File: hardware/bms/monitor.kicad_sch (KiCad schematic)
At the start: 116 parts, among them Q2 Q_PMOS_GDS, Q3 Q_PMOS_GDS, U1 BQ76952

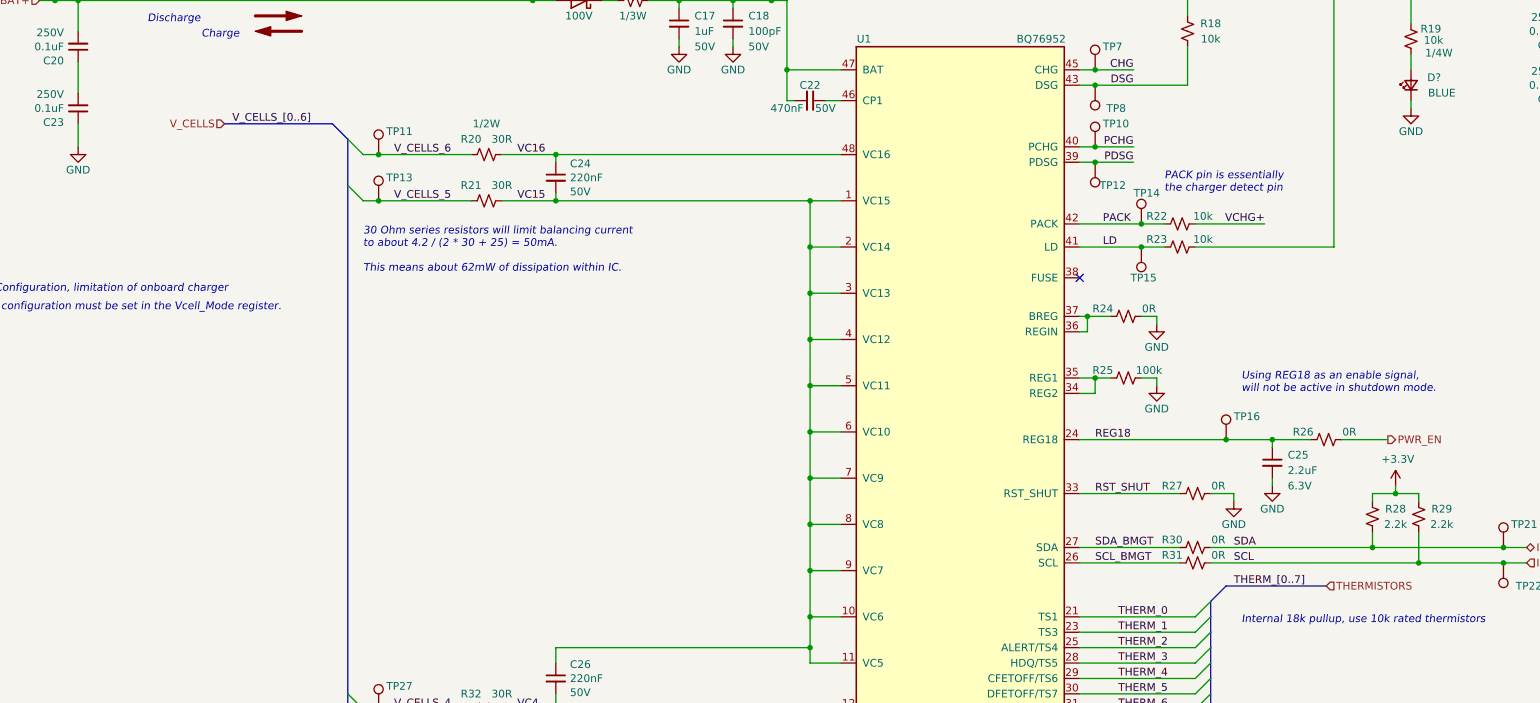
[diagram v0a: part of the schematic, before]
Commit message: Updated USB C connector, fixed all sch ERC errors, imported footprints into pcb file, fixed any pcb import errors.
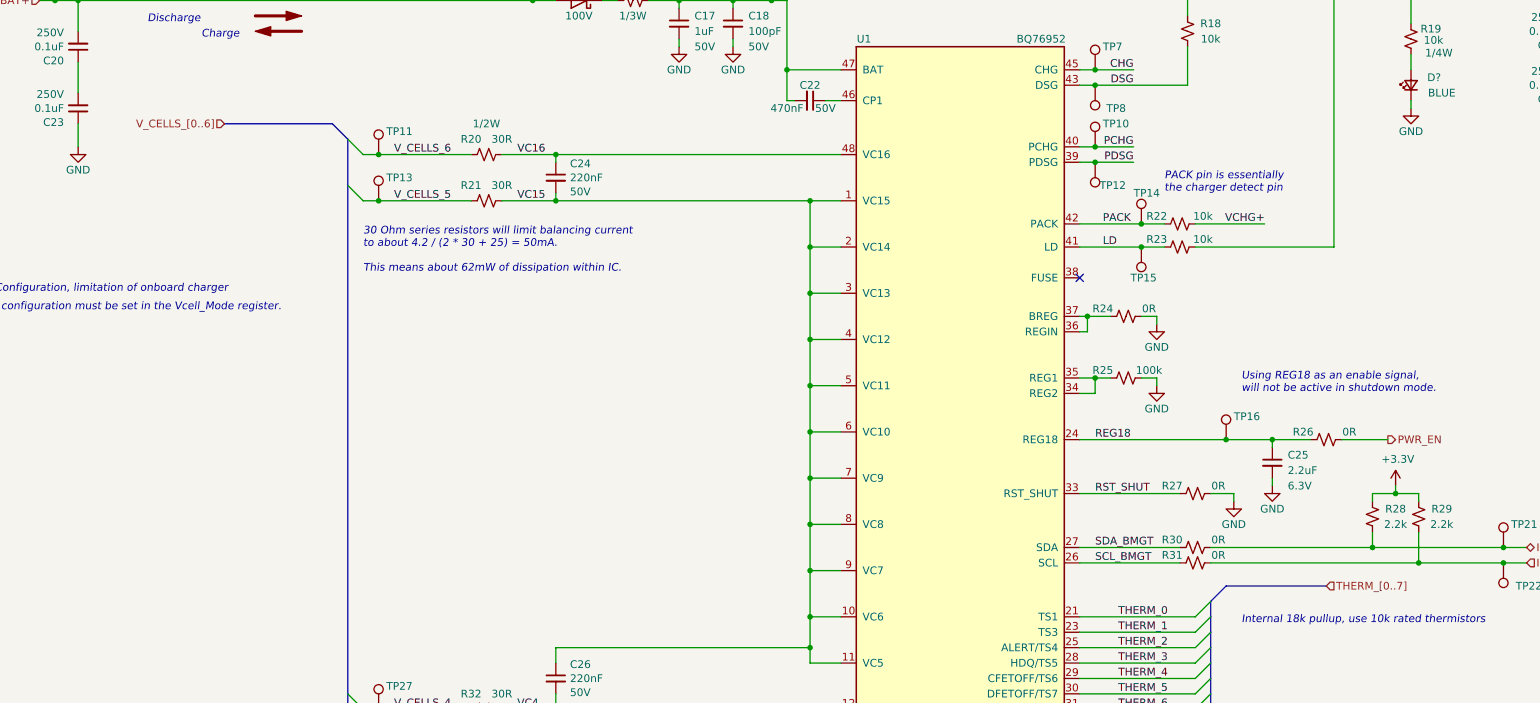
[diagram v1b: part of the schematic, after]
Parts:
- C24, C26, C31, C32, C38, C39, C40: footprint (none) -> Capacitor_SMD:C_0603_1608Metric

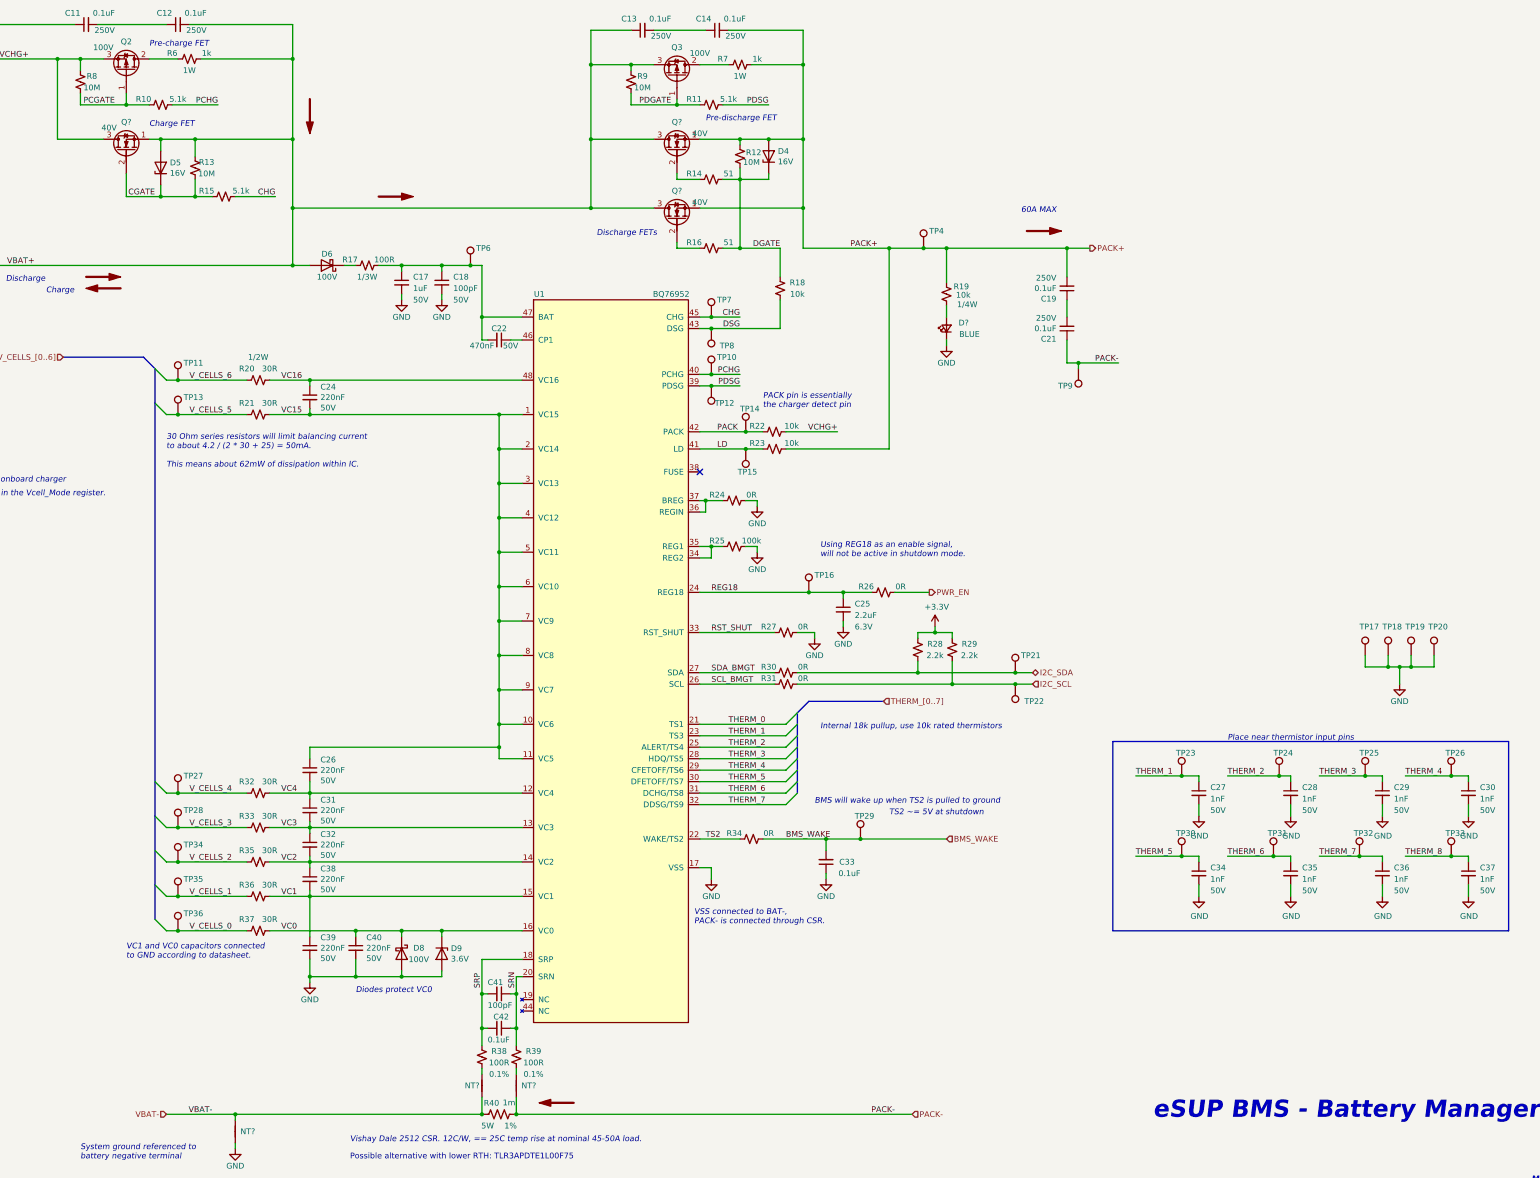
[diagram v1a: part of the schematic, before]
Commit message: Sch cleanup, added extra netties
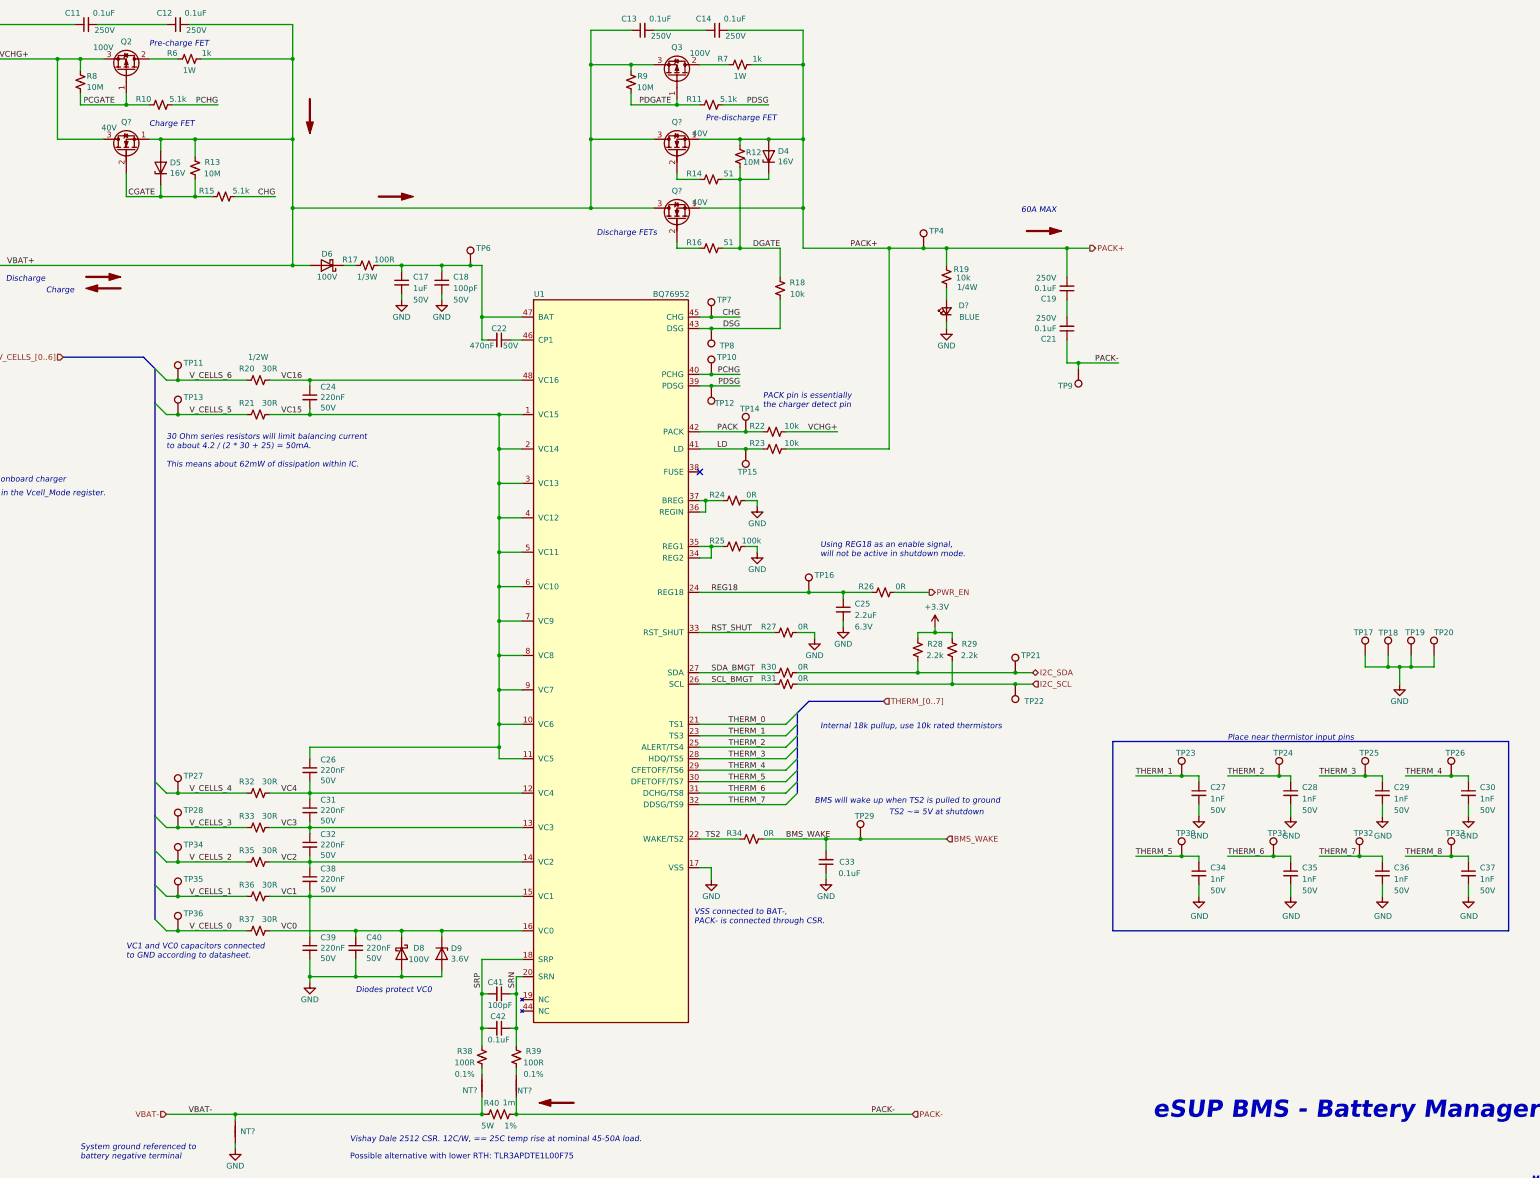
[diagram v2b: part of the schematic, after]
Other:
- moved on the sheet: D?, R19
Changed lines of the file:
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@@
     (stroke (width 0) (type default))
   )
-  (wire (pts (xy 264.16 91.44) (xy 264.16 92.71))
+  (wire (pts (xy 264.16 87.63) (xy 264.16 88.9))
     (stroke (width 0) (type default))
   )
@@
     (stroke (width 0) (type default))
   )
-  (wire (pts (xy 264.16 83.82) (xy 264.16 86.36))
+  (wire (pts (xy 264.16 80.01) (xy 264.16 82.55))
     (stroke (width 0) (type default))
   )
@@
     (stroke (width 0) (type default))
   )
-  (wire (pts (xy 264.16 71.12) (xy 264.16 78.74))
+  (wire (pts (xy 264.16 71.12) (xy 264.16 74.93))
     (stroke (width 0) (type default))
   )
@@
   (symbol (lib_id "Device:R_Small_US") (at 97.79 53.34 0) (unit 1)
     (in_bom yes) (on_board yes) (dnp no)
-    (property "Reference" "R13" (at 100.33 52.07 0)
+    (property "Reference" "R13" (at 101.6 52.07 0)
       (effects (font (size 1.27 1.27)))
     )
-    (property "Value" "10M" (at 100.33 54.61 0)
+    (property "Value" "10M" (at 101.6 54.61 0)
       (effects (font (size 1.27 1.27)))
     )
@@
       (effects (font (size 1.27 1.27)))
     )
-    (property "Value" "10M" (at 196.85 35.56 0)
+    (property "Value" "10M" (at 197.481 35.5436 0)
       (effects (font (size 1.27 1.27)))
     )
@@
       (effects (font (size 1.27 1.27)))
     )
-    (property "Value" "10M" (at 74.93 35.56 0)
+    (property "Value" "10M" (at 75.6257 35.471 0)
       (effects (font (size 1.27 1.27)))
     )
@@
   (symbol (lib_id "Device:R_Small_US") (at 161.29 250.19 0) (unit 1)
     (in_bom yes) (on_board yes) (dnp no)
-    (property "Reference" "R38" (at 165.1 248.92 0)
+    (property "Reference" "R38" (at 157.48 248.92 0)
       (effects (font (size 1.27 1.27)))
     )
-    (property "Value" "100R" (at 165.1 251.46 0)
+    (property "Value" "100R" (at 157.48 251.46 0)
       (effects (font (size 1.27 1.27)))
     )
@@
       (effects (font (size 1.27 1.27)) hide)
     )
-    (property "Tolerance" "0.1%" (at 165.1 254 0)
+    (property "Tolerance" "0.1%" (at 157.48 254 0)
       (effects (font (size 1.27 1.27)))
     )
@@
   (symbol (lib_id "bms-rescue:Net-Tie_2-Device") (at 161.29 256.54 270) (unit 1)
     (in_bom yes) (on_board yes) (dnp no)
-    (property "Reference" "NT?" (at 157.48 256.54 90)
+    (property "Reference" "NT?" (at 156.9946 257.6077 90)
       (effects (font (size 1.27 1.27)) (justify left))
     )
@@
   (symbol (lib_id "bms-rescue:Net-Tie_2-Device") (at 168.91 256.54 270) (unit 1)
     (in_bom yes) (on_board yes) (dnp no)
-    (property "Reference" "NT?" (at 170.0276 256.54 90)
+    (property "Reference" "NT?" (at 169.0954 257.6724 90)
       (effects (font (size 1.27 1.27)) (justify left))
     )
@@
   (symbol (lib_id "Device:C_Small") (at 165.1 243.84 270) (unit 1)
     (in_bom yes) (on_board yes) (dnp no)
-    (property "Reference" "C42" (at 163.83 241.3 90)
+    (property "Reference" "C42" (at 163.1505 241.2192 90)
       (effects (font (size 1.27 1.27)) (justify left))
     )
@@
     )
   )
-  (symbol (lib_id "power:GND") (at 264.16 92.71 0) (unit 1)
+  (symbol (lib_id "power:GND") (at 264.16 88.9 0) (unit 1)
     (in_bom yes) (on_board yes) (dnp no)
-    (property "Reference" "#PWR049" (at 264.16 99.06 0)
+    (property "Reference" "#PWR049" (at 264.16 95.25 0)
       (effects (font (size 1.27 1.27)) hide)
     )
-    (property "Value" "GND" (at 264.16 96.52 0)
+    (property "Value" "GND" (at 264.16 92.71 0)
       (effects (font (size 1.27 1.27)))
     )
-    (property "Footprint" "" (at 264.16 92.71 0)
+    (property "Footprint" "" (at 264.16 88.9 0)
       (effects (font (size 1.27 1.27)) hide)
     )
-    (property "Datasheet" "" (at 264.16 92.71 0)
+    (property "Datasheet" "" (at 264.16 88.9 0)
       (effects (font (size 1.27 1.27)) hide)
     )
@@
   (symbol (lib_id "Connector:TestPoint") (at 372.11 161.29 0) (unit 1)
     (in_bom yes) (on_board yes) (dnp no)
-    (property "Reference" "TP20" (at 370.84 154.94 0)
+    (property "Reference" "TP20" (at 372.11 156.21 0)
       (effects (font (size 1.27 1.27)) (justify left))
     )
@@
   (symbol (lib_id "Connector:TestPoint") (at 361.95 161.29 0) (unit 1)
     (in_bom yes) (on_board yes) (dnp no)
-    (property "Reference" "TP18" (at 360.68 154.94 0)
+    (property "Reference" "TP18" (at 359.8153 156.2748 0)
       (effects (font (size 1.27 1.27)) (justify left))
     )
@@
     )
   )
-  (symbol (lib_id "Device:LED_Small") (at 264.16 88.9 90) (unit 1)
+  (symbol (lib_id "Device:LED_Small") (at 264.16 85.09 90) (unit 1)
     (in_bom yes) (on_board yes) (dnp no)
-    (property "Reference" "D?" (at 267.97 87.63 90)
+    (property "Reference" "D?" (at 267.97 83.82 90)
       (effects (font (size 1.27 1.27)))
     )
-    (property "Value" "BLUE" (at 269.24 90.17 90)
+    (property "Value" "BLUE" (at 269.24 86.36 90)
       (effects (font (size 1.27 1.27)))
     )
-    (property "Footprint" "LED_SMD:LED_0603_1608Metric" (at 264.16 88.9 90)
+    (property "Footprint" "LED_SMD:LED_0603_1608Metric" (at 264.16 85.09 90)
       (effects (font (size 1.27 1.27)) hide)
     )
-    (property "Datasheet" "~" (at 264.16 88.9 90)
+    (property "Datasheet" "~" (at 264.16 85.09 90)
       (effects (font (size 1.27 1.27)) hide)
     )
-    (property "MFG" "Würth Elektronik" (at 264.16 88.9 90)
+    (property "MFG" "Würth Elektronik" (at 264.16 85.09 90)
       (effects (font (size 1.27 1.27)) hide)
     )
-    (property "MFG PN" "150060BS75000" (at 264.16 88.9 90)
+    (property "MFG PN" "150060BS75000" (at 264.16 85.09 90)
       (effects (font (size 1.27 1.27)) hide)
     )
-    (property "VF" "3.2V" (at 264.16 88.9 90)
+    (property "VF" "3.2V" (at 264.16 85.09 90)
       (effects (font (size 1.27 1.27)) hide)
     )
@@
   (symbol (lib_id "Connector:TestPoint") (at 367.03 161.29 0) (unit 1)
     (in_bom yes) (on_board yes) (dnp no)
-    (property "Reference" "TP19" (at 365.76 154.94 0)
+    (property "Reference" "TP19" (at 365.76 156.21 0)
       (effects (font (size 1.27 1.27)) (justify left))
     )
@@
     )
   )
-  (symbol (lib_id "Device:R_Small_US") (at 264.16 81.28 0) (unit 1)
+  (symbol (lib_id "Device:R_Small_US") (at 264.16 77.47 0) (unit 1)
     (in_bom yes) (on_board yes) (dnp no)
-    (property "Reference" "R19" (at 267.4354 79.6169 0)
+    (property "Reference" "R19" (at 267.4354 75.8069 0)
       (effects (font (size 1.27 1.27)))
     )
-    (property "Value" "10k" (at 267.8757 81.4756 0)
+    (property "Value" "10k" (at 267.8757 77.6656 0)
       (effects (font (size 1.27 1.27)))
     )
-    (property "Footprint" "Resistor_SMD:R_0603_1608Metric" (at 264.16 81.28 0)
+    (property "Footprint" "Resistor_SMD:R_0603_1608Metric" (at 264.16 77.47 0)
       (effects (font (size 1.27 1.27)) hide)
     )
-    (property "Datasheet" "~" (at 264.16 81.28 0)
+    (property "Datasheet" "~" (at 264.16 77.47 0)
       (effects (font (size 1.27 1.27)) hide)
     )
-    (property "MFG" "Panasonic Electronic Components" (at 264.16 81.28 90)
+    (property "MFG" "Panasonic Electronic Components" (at 264.16 77.47 90)
       (effects (font (size 1.27 1.27)) hide)
     )
-    (property "MFG PN" "ERJ-UP3F1002V" (at 264.16 81.28 90)
+    (property "MFG PN" "ERJ-UP3F1002V" (at 264.16 77.47 90)
       (effects (font (size 1.27 1.27)) hide)
     )
-    (property "Power" "1/4W" (at 268.7561 83.5789 0)
+    (property "Power" "1/4W" (at 268.7561 79.7689 0)
       (effects (font (size 1.27 1.27)))
     )
@@
   (symbol (lib_id "Connector:TestPoint") (at 356.87 161.29 0) (unit 1)
     (in_bom yes) (on_board yes) (dnp no)
-    (property "Reference" "TP17" (at 355.6 154.94 0)
+    (property "Reference" "TP17" (at 354.33 156.21 0)
       (effects (font (size 1.27 1.27)) (justify left))
     )

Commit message: Continued layout, defined board area based on mech assembly
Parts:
- removed NT?: Net-Tie, NetTie:NetTie-2_SMD_Pad2.0mm, symbol bms-rescue:Net-Tie_2-Device
- R20, R21, R32, R33, R35, R36, R37: footprint Resistor_SMD:R_1210_3225Metric -> Resistor_SMD:R_0805_2012Metric; MFG PN ERJ-P14J300U -> ERJ-P06J300V
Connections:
- net VBAT- is gone; now on net GND: NT?.2, R40.2

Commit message: Updated test points to 0.5mm to save space, continued layout
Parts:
- NT? (x2): now left out of the parts list
- TP10, TP11, TP12, TP13, TP14, TP15, TP16, TP17, TP18, TP19, TP20, TP21, TP22, TP23, TP24, TP25, TP26, TP27, TP28, TP29, TP3, TP30, TP31, TP32, TP33, TP34, TP35, TP36, TP4, TP5, TP6, TP7, TP8, TP9: footprint TestPoint:TestPoint_Pad_D1.0mm -> bms:TestPoint_Pad_D0.5mm; now left out of the parts list
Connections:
- net THERM_8 is gone; now on net THERM_0: C37.1, TP33.1

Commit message: More layout, changed precharge / predischarged PMOS selection to SOT-23 size to save space. Charger layout will be difficult, may need to change charger input terminal location...
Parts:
- removed C15, C16: 0.1uF, Capacitor_SMD:C_0805_2012Metric, symbol Device:C_Small
- removed Q2, Q3: Q_PMOS_GDS, Package_TO_SOT_SMD:SOT-223-3_TabPin2, symbol Device:Q_PMOS_GDS
- added Q2, Q3: Q_PMOS_GSD, Package_TO_SOT_SMD:SOT-23, symbol Device:Q_PMOS_GSD
- D4, D5: footprint Diode_SMD:D_SOD-123 -> Diode_SMD:D_SOD-523; MFG PN SZMMSZ5246BT1G -> SZMM5Z16VT1G
- NT? (x2): footprint NetTie:NetTie-2_SMD_Pad0.5mm -> bms:NetTie-2_SMD_Pad_8mil
- R6, R7: MFG Panasonic Electronic Components -> TE Connectivity Passive Product; MFG PN ERJ-1TNF1001U -> CRGP2512F1K0; Power 1W -> 2W
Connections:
- net PCGATE: now also Q2.1 (G)
- net PDGATE: now also Q3.1 (G)
- net VBAT+: now also Q3.2 (S)
- net VCHG+: now also Q2.2 (S)
- net at R7.1: now also Q3.3 (D)
- net at R6.1: now also Q2.3 (D)
